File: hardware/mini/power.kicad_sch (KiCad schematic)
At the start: 40 parts, among them U1 INA226, U2 TPS55289

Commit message: route power stage
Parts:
- removed C22: 47u, Capacitor_SMD:CP_Elec_8x10.5, symbol Device:C_Polarized
- removed NT2: NetTie_2, NetTie:NetTie-2_SMD_Pad0.5mm, symbol Device:NetTie_2
- removed R7: 100k, Resistor_SMD:R_0402_1005Metric, symbol Device:R
- added C77: 270u 35V, Capacitor_SMD:CP_Elec_10x10, symbol Device:C_Polarized
- C1: value 47u -> 270u 35V; footprint Capacitor_SMD:CP_Elec_8x10.5 -> Capacitor_SMD:CP_Elec_10x10; LCSC C5246568 -> C5246557
- L1: footprint Inductor_SMD:L_Changjiang_FXL1050 -> protovolt_mini_fp:L_SOREDE_SRTC.1010; LCSC C5359261 -> C7427509
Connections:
- net GND: no longer C8.2
- net GNDPWR: now also C8.2, C77.2
- net IS+: now also C77.1
- net FB renamed CONVERTER_~{INT}
- net SENSE_INT renamed SENSE_~{INT}

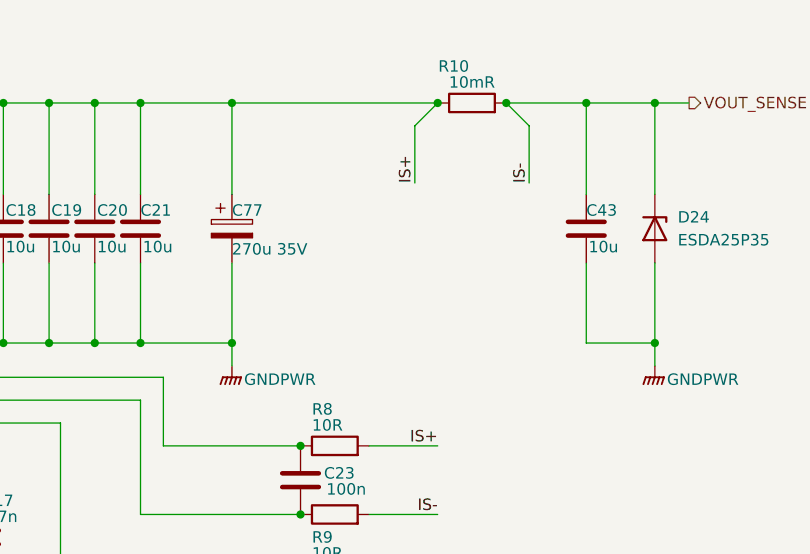
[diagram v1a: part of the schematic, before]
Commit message: route digitals
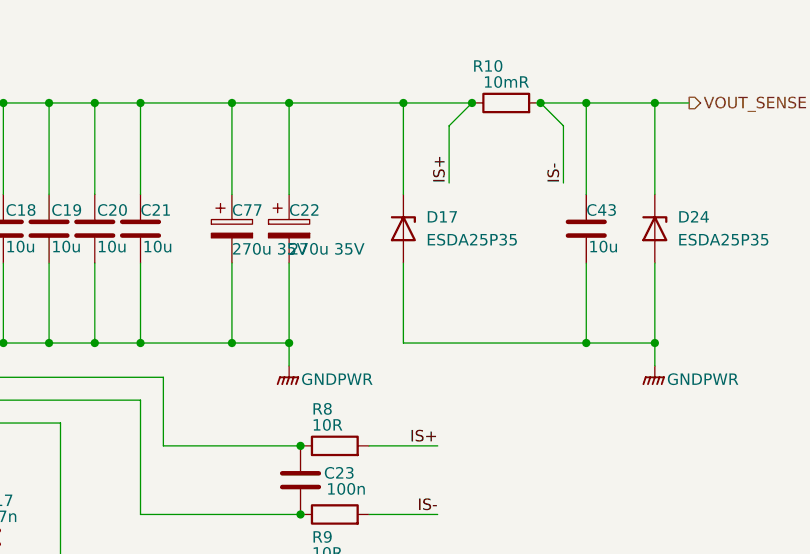
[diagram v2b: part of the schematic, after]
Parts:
- added C22: 270u 35V, Capacitor_SMD:CP_Elec_10x10, symbol Device:C_Polarized
- added D17: ESDA25P35, protovolt_mini_fp:D_1610_4027Metric, symbol Device:D_Zener
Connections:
- net GNDPWR: now also C22.2, D17.2 (A)
- net IS+: now also C22.1, D17.1 (K)
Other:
- moved on the sheet: R10

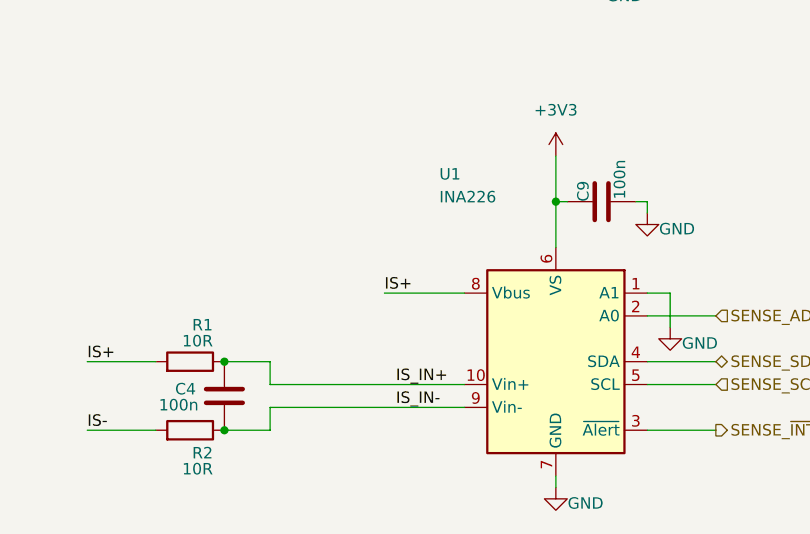
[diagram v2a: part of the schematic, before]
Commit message: route sense lines
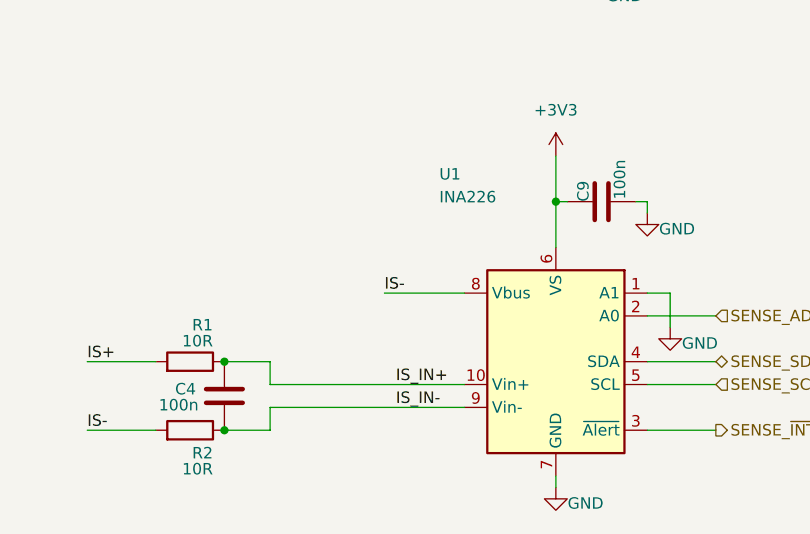
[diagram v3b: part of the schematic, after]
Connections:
- net IS+: no longer U1.8 (Vbus)
- net VOUT_SENSE: now also U1.8 (Vbus)
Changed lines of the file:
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@@
-	)
-	(label "IS+"
-		(at 69.85 138.43 0)
-		(effects
-			(font
-				(size 1.27 1.27)
-			)
-			(justify left bottom)
-		)
 	)
 	(label "IS+"
@@
 		)
 	)
+	(label "IS-"
+		(at 69.85 138.43 0)
+		(effects
+			(font
+				(size 1.27 1.27)
+			)
+			(justify left bottom)
+		)
+	)

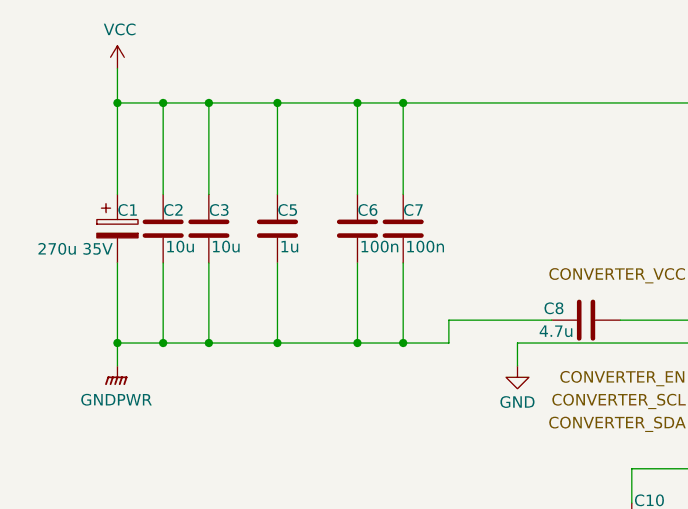
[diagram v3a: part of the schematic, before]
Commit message: put FPC to front & rearrange buck/boost
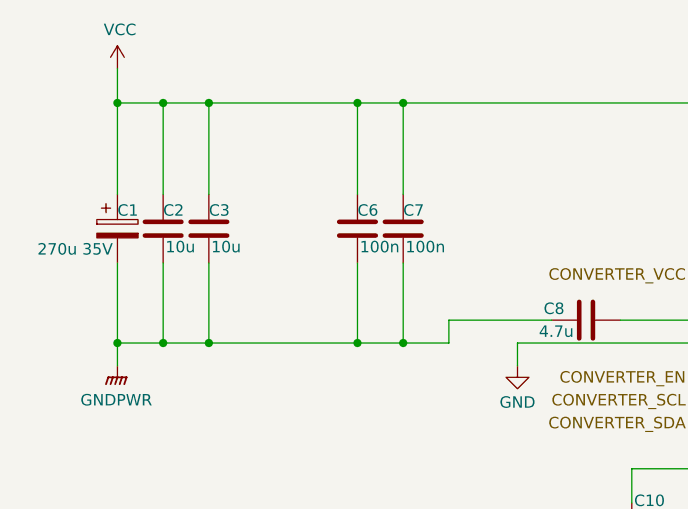
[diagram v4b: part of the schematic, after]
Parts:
- removed C5: 1u, Capacitor_SMD:C_1206_3216Metric, symbol Device:C
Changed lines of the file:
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@@
 	)
 	(junction
-		(at 57.15 45.72)
-		(diameter 0)
-		(color 0 0 0 0)
-	)
-	(junction
 		(at 161.29 72.39)
 		(diameter 0)
@@
 	)
 	(junction
-		(at 57.15 72.39)
-		(diameter 0)
-		(color 0 0 0 0)
-	)
-	(junction
 		(at 139.7 43.18)
 		(diameter 0)
@@
 	(wire
 		(pts
-			(xy 57.15 45.72) (xy 66.04 45.72)
+			(xy 49.53 45.72) (xy 66.04 45.72)
 		)
 		(stroke
@@
 	(wire
 		(pts
-			(xy 57.15 72.39) (xy 66.04 72.39)
+			(xy 49.53 72.39) (xy 66.04 72.39)
 		)
 		(stroke
@@
 	(wire
 		(pts
-			(xy 57.15 63.5) (xy 57.15 72.39)
-		)
-		(stroke
-			(width 0)
-			(type default)
-		)
-	)
-	(wire
-		(pts
 			(xy 184.15 45.72) (xy 184.15 55.88)
 		)
@@
 	(wire
 		(pts
-			(xy 49.53 45.72) (xy 57.15 45.72)
-		)
-		(stroke
-			(width 0)
-			(type default)
-		)
-	)
-	(wire
-		(pts
 			(xy 228.6 48.26) (xy 231.14 45.72)
 		)
@@
 	(wire
 		(pts
-			(xy 57.15 45.72) (xy 57.15 55.88)
-		)
-		(stroke
-			(width 0)
-			(type default)
-		)
-	)
-	(wire
-		(pts
 			(xy 184.15 72.39) (xy 179.07 72.39)
 		)
@@
 	(wire
 		(pts
-			(xy 49.53 72.39) (xy 57.15 72.39)
-		)
-		(stroke
-			(width 0)
-			(type default)
-		)
-	)
-	(wire
-		(pts
 			(xy 185.42 81.28) (xy 185.42 105.41)
 		)
@@
 					(unit 1)
 				)
-			)
-		)
-	)
-	(symbol
-		(lib_id "Device:C")
-		(at 57.15 59.69 0)
-		(unit 1)
-		(exclude_from_sim no)
-		(in_bom yes)
-		(on_board yes)
-		(dnp no)
-		(property "Reference" "C5"
-			(at 57.15 57.658 0)
-			(effects
-				(font
-					(size 1.27 1.27)
-				)
-				(justify left)
-			)
-		)
-		(property "Value" "1u"
-			(at 57.404 61.7221 0)
-			(effects
-				(font
-					(size 1.27 1.27)
-				)
-				(justify left)
-			)
-		)
-		(property "Footprint" "Capacitor_SMD:C_1206_3216Metric"
-			(at 58.1152 63.5 0)
-			(effects
-				(font
-					(size 1.27 1.27)
-				)
-				(hide yes)
-			)
-		)
-		(property "Datasheet" "~"
-			(at 57.15 59.69 0)
-			(effects
-				(font
-					(size 1.27 1.27)
-				)
-				(hide yes)
-			)
-		)
-		(property "Description" "Unpolarized capacitor"
-			(at 57.15 59.69 0)
-			(effects
-				(font
-					(size 1.27 1.27)
-				)
-				(hide yes)
-			)
-		)
-		(property "LCSC" "C1848"
-			(at 57.15 59.69 0)
-			(effects
-				(font
-					(size 1.27 1.27)
-				)
-				(hide yes)
-			)
-		)
-		(pin "2"
-		)
-		(pin "1"
-		)
-		(instances
-			(project "mini"
-				(path "/5aaaac9a-5acd-4aef-ad51-a6d04aa88705/2f5f237b-0f73-4b73-a622-46731dbdbc6c"
-					(reference "C5")
-					(unit 1)
-				)
-				(path "/5aaaac9a-5acd-4aef-ad51-a6d04aa88705/2f6f259a-8708-4cff-b8be-2da8284c0274"
-					(reference "C48")
-					(unit 1)
-				)

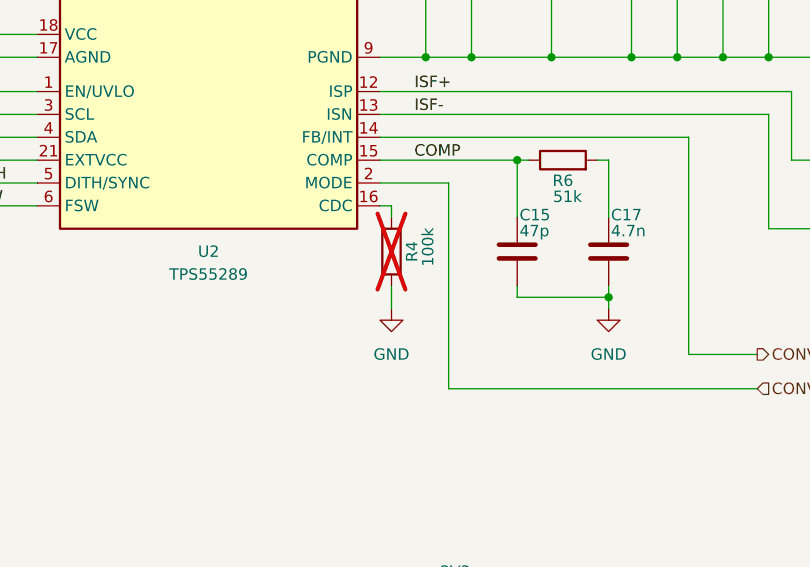
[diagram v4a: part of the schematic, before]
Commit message: route power
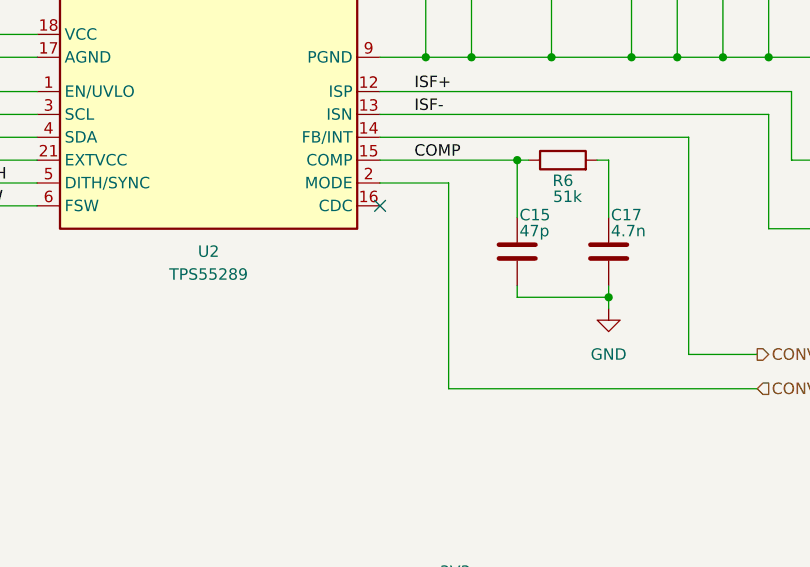
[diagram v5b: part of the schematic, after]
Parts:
- removed R4: 100k, Resistor_SMD:R_0402_1005Metric, symbol Device:R
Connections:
- no-connect marks 0 -> 1
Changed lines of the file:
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@@
 		(color 0 0 0 0)
 	)
+	(no_connect
+		(at 151.13 88.9)
+	)
 	(wire
 		(pts
@@
 	(wire
 		(pts
-			(xy 152.4 88.9) (xy 152.4 90.17)
-		)
-		(stroke
-			(width 0)
-			(type default)
-		)
-	)
-	(wire
-		(pts
 			(xy 184.15 63.5) (xy 184.15 72.39)
 		)
@@
 	(wire
 		(pts
-			(xy 152.4 97.79) (xy 152.4 100.33)
-		)
-		(stroke
-			(width 0)
-			(type default)
-		)
-	)
-	(wire
-		(pts
 			(xy 97.79 128.27) (xy 99.06 128.27)
 		)
@@
 		(pts
 			(xy 251.46 45.72) (xy 251.46 55.88)
-		)
-		(stroke
-			(width 0)
-			(type default)
-		)
-	)
-	(wire
-		(pts
-			(xy 151.13 88.9) (xy 152.4 88.9)
 		)
 		(stroke
@@
 	(symbol
 		(lib_id "Device:R")
-		(at 152.4 93.98 180)
-		(unit 1)
-		(exclude_from_sim no)
-		(in_bom yes)
-		(on_board yes)
-		(dnp yes)
-		(property "Reference" "R4"
-			(at 154.686 93.98 90)
-			(effects
-				(font
-					(size 1.27 1.27)
-				)
-			)
-		)
-		(property "Value" "100k"
-			(at 156.464 93.472 90)
-			(effects
-				(font
-					(size 1.27 1.27)
-				)
-			)
-		)
-		(property "Footprint" "Resistor_SMD:R_0402_1005Metric"
-			(at 154.178 93.98 90)
-			(effects
-				(font
-					(size 1.27 1.27)
-				)
-				(hide yes)
-			)
-		)
-		(property "Datasheet" "~"
-			(at 152.4 93.98 0)
-			(effects
-				(font
-					(size 1.27 1.27)
-				)
-				(hide yes)
-			)
-		)
-		(property "Description" "Resistor"
-			(at 152.4 93.98 0)
-			(effects
-				(font
-					(size 1.27 1.27)
-				)
-				(hide yes)
-			)
-		)
-		(property "LCSC" "C25741"
-			(at 152.4 93.98 0)
-			(effects
-				(font
-					(size 1.27 1.27)
-				)
-				(hide yes)
-			)
-		)
-		(pin "1"
-		)
-		(pin "2"
-		)
-		(instances
-			(project "mini"
-				(path "/5aaaac9a-5acd-4aef-ad51-a6d04aa88705/2f5f237b-0f73-4b73-a622-46731dbdbc6c"
-					(reference "R4")
-					(unit 1)
-				)
-				(path "/5aaaac9a-5acd-4aef-ad51-a6d04aa88705/2f6f259a-8708-4cff-b8be-2da8284c0274"
-					(reference "R30")
-					(unit 1)
-				)
-			)
-		)
-	)
-	(symbol
-		(lib_id "Device:R")
 		(at 102.87 93.98 0)
 		(unit 1)
@@
 					(unit 1)
 				)
-			)
-		)
-	)
-	(symbol
-		(lib_id "power:GND")
-		(at 152.4 100.33 0)
-		(unit 1)
-		(exclude_from_sim no)
-		(in_bom yes)
-		(on_board yes)
-		(dnp no)
-		(fields_autoplaced yes)
-		(property "Reference" "#PWR016"
-			(at 152.4 106.68 0)
-			(effects
-				(font
-					(size 1.27 1.27)
-				)
-				(hide yes)
-			)
-		)
-		(property "Value" "GND"
-			(at 152.4 105.41 0)
-			(effects
-				(font
-					(size 1.27 1.27)
-				)
-			)
-		)
-		(property "Footprint" ""
-			(at 152.4 100.33 0)
-			(effects
-				(font
-					(size 1.27 1.27)
-				)
-				(hide yes)
-			)
-		)
-		(property "Datasheet" ""
-			(at 152.4 100.33 0)
-			(effects
-				(font
-					(size 1.27 1.27)
-				)
-				(hide yes)
-			)
-		)
-		(property "Description" "Power symbol creates a global label with name \"GND\" , ground"
-			(at 152.4 100.33 0)
-			(effects
-				(font
-					(size 1.27 1.27)
-				)
-				(hide yes)
-			)
-		)
-		(pin "1"
-		)
-		(instances
-			(project "mini"
-				(path "/5aaaac9a-5acd-4aef-ad51-a6d04aa88705/2f5f237b-0f73-4b73-a622-46731dbdbc6c"
-					(reference "#PWR016")
-					(unit 1)
-				)
-				(path "/5aaaac9a-5acd-4aef-ad51-a6d04aa88705/2f6f259a-8708-4cff-b8be-2da8284c0274"
-					(reference "#PWR054")
-					(unit 1)
-				)

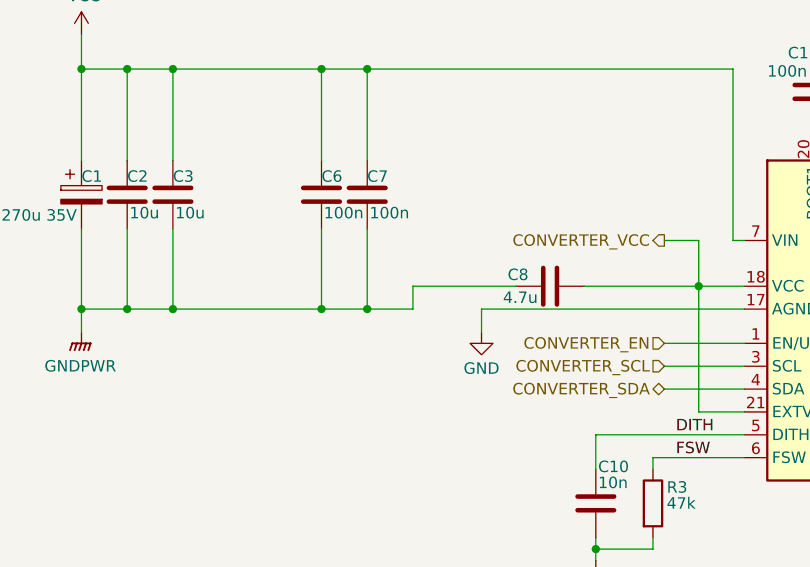
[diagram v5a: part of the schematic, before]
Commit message: reroute all except 3V3 & GND
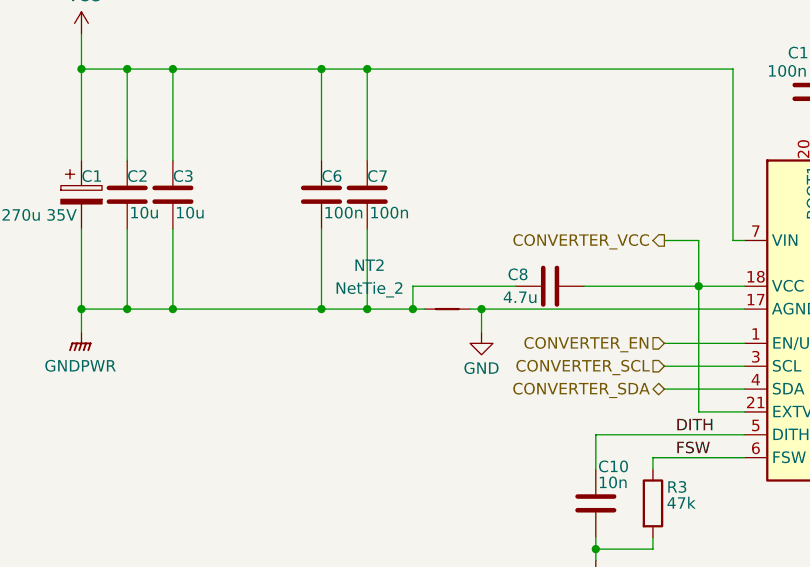
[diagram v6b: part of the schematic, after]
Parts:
- added NT2: NetTie_2, NetTie:NetTie-2_SMD_Pad0.5mm, symbol Device:NetTie_2
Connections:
- net GND: now also NT2.2
- net GNDPWR: now also NT2.1
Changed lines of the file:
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@@
 	)
 	(junction
+		(at 76.2 72.39)
+		(diameter 0)
+		(color 0 0 0 0)
+	)
+	(junction
 		(at 66.04 45.72)
 		(diameter 0)
@@
 	)
 	(junction
+		(at 83.82 72.39)
+		(diameter 0)
+		(color 0 0 0 0)
+	)
+	(junction
 		(at 39.37 72.39)
 		(diameter 0)
@@
 	(wire
 		(pts
+			(xy 76.2 72.39) (xy 77.47 72.39)
+		)
+		(stroke
+			(width 0)
+			(type default)
+		)
+	)
+	(wire
+		(pts
 			(xy 194.31 72.39) (xy 189.23 72.39)
 		)
@@
 	(wire
 		(pts
+			(xy 82.55 72.39) (xy 83.82 72.39)
+		)
+		(stroke
+			(width 0)
+			(type default)
+		)
+	)
+	(wire
+		(pts
 			(xy 170.18 63.5) (xy 170.18 72.39)
 		)
@@
 					(unit 1)
 				)
+			)
+		)
+	)
+	(symbol
+		(lib_id "Device:NetTie_2")
+		(at 80.01 72.39 0)
+		(unit 1)
+		(exclude_from_sim no)
+		(in_bom no)
+		(on_board yes)
+		(dnp no)
+		(property "Reference" "NT2"
+			(at 71.374 67.564 0)
+			(effects
+				(font
+					(size 1.27 1.27)
+				)
+			)
+		)
+		(property "Value" "NetTie_2"
+			(at 71.374 70.104 0)
+			(effects
+				(font
+					(size 1.27 1.27)
+				)
+			)
+		)
+		(property "Footprint" "NetTie:NetTie-2_SMD_Pad0.5mm"
+			(at 80.01 72.39 0)
+			(effects
+				(font
+					(size 1.27 1.27)
+				)
+				(hide yes)
+			)
+		)
+		(property "Datasheet" "~"
+			(at 80.01 72.39 0)
+			(effects
+				(font
+					(size 1.27 1.27)
+				)
+				(hide yes)
+			)
+		)
+		(property "Description" "Net tie, 2 pins"
+			(at 80.01 72.39 0)
+			(effects
+				(font
+					(size 1.27 1.27)
+				)
+				(hide yes)
+			)
+		)
+		(pin "2"
+		)
+		(pin "1"
+		)
+		(instances
+			(project "mini"
+				(path "/5aaaac9a-5acd-4aef-ad51-a6d04aa88705/2f5f237b-0f73-4b73-a622-46731dbdbc6c"
+					(reference "NT2")
+					(unit 1)
+				)
+				(path "/5aaaac9a-5acd-4aef-ad51-a6d04aa88705/2f6f259a-8708-4cff-b8be-2da8284c0274"
+					(reference "NT3")
+					(unit 1)
+				)

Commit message: finish routing
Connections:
- net GND: no longer C10.2, C15.2, C17.2, NT2.2, R3.2, U2.17 (AGND)
- new net GNDA: C10.2, C15.2, C17.2, NT2.2, R3.2, U2.17 (AGND)

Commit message: cleanup schematic
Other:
- title: (none) -> Protovolt MINI
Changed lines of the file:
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@@
 	(generator_version "9.0")
 	(paper "A4")
+	(title_block
+		(title "Protovolt MINI")
+		(date "2025-06-16")
+		(rev "A")
+		(comment 3 "MINI")
+		(comment 4 "Protovolt")
+	)
 	(text "Place next to\nTPS55829"
 		(exclude_from_sim no)
